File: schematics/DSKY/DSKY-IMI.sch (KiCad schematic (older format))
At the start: 3 parts, among them J103 Conn_02x08, J104 Conn_02x10, U201 74LS32

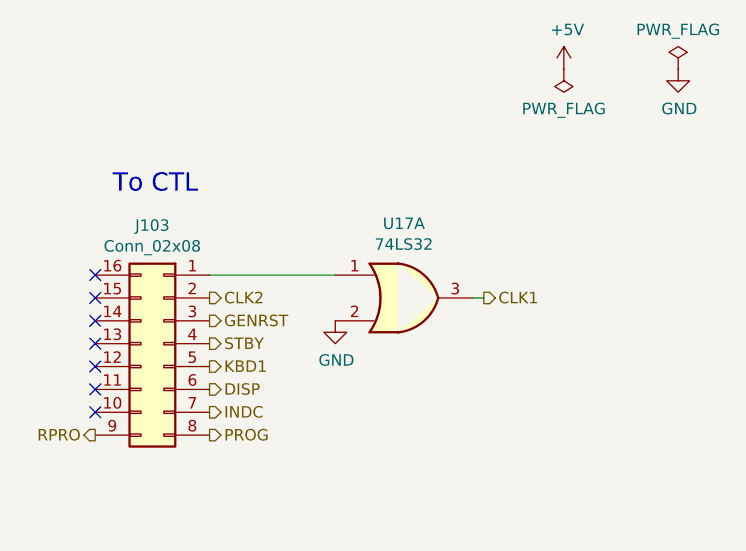
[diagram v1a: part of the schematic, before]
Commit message: Minor tweaks to the display decoding logic.
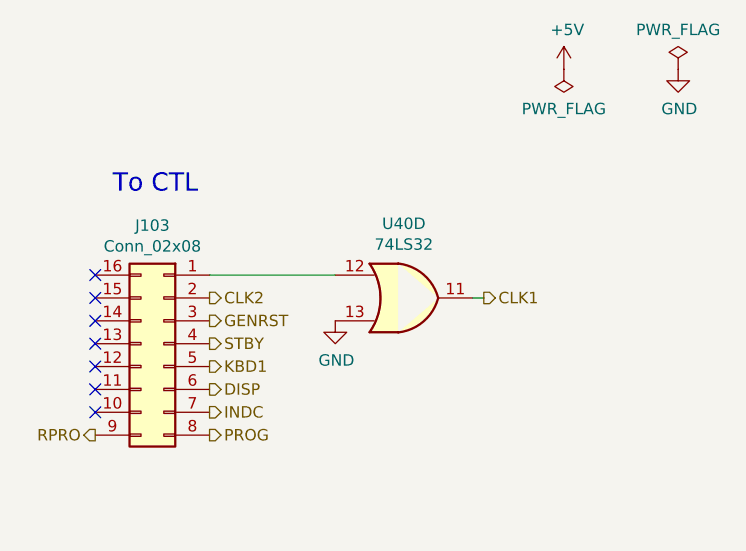
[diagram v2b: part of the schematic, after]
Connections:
- net CLK1: now also U201.11; no longer U201.3
- net GND: now also U201.13; no longer U201.2
- net at J103.1 (Pin_1): now also U201.12; no longer U201.1
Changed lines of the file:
@@
 $Comp
 L 74xx:74LS32 U201
-U 1 1 5F6065A8
+U 4 1 5F6065A8
 P 8400 2000
 AR Path="/5F5E4E3B/5F5F82D4/5F6065A8" Ref="U201"  Part="1"
-AR Path="/60F989FD/5F6065A8" Ref="U17"  Part="1"
-F 0 "U17" H 8400 2325 50  0000 C CNN
+AR Path="/60F989FD/5F6065A8" Ref="U40"  Part="4"
+F 0 "U40" H 8400 2325 50  0000 C CNN
 F 1 "74LS32" H 8400 2234 50  0000 C CNN
 F 2 "" H 8400 2000 50  0001 C CNN
 F 3 "http://www.ti.com/lit/gpn/sn74LS32" H 8400 2000 50  0001 C CNN
-	1    8400 2000
+	4    8400 2000
 	1    0    0    -1
 $EndComp

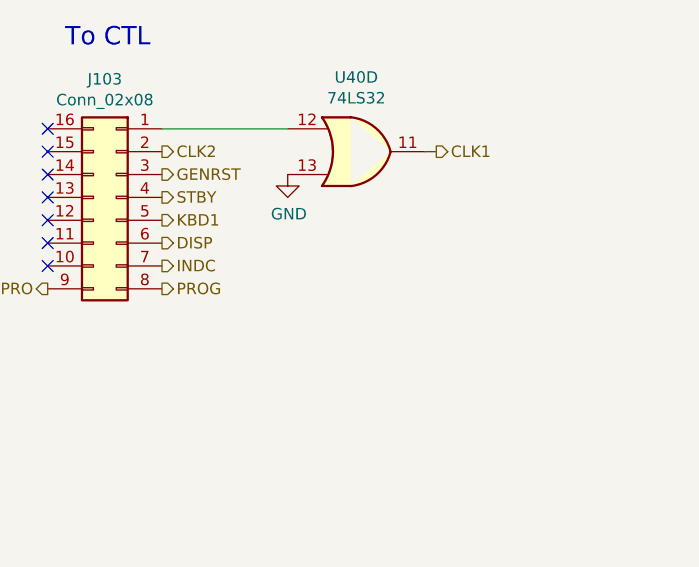
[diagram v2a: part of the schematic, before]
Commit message: Simplified reset lines.
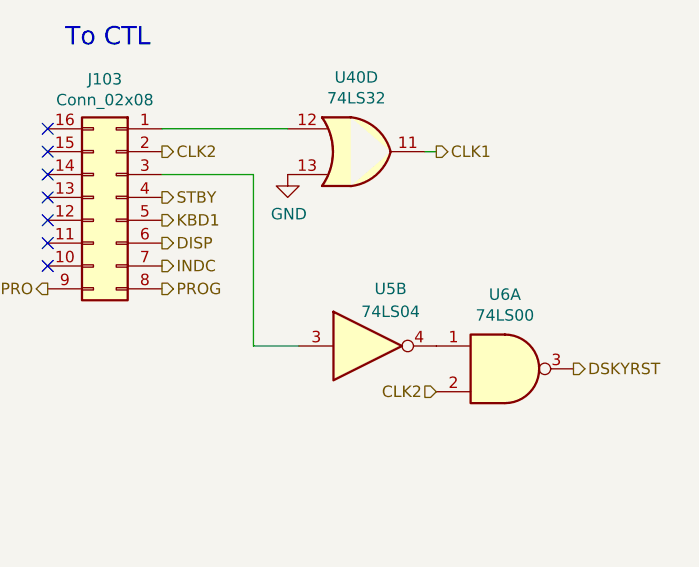
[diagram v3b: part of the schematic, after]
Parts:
- added U5: 74LS04, symbol 74xx:74LS04
- added U6: 74LS00, symbol 74xx:74LS00
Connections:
- net CLK2: now also U6.2
- net GENRST: no longer names the net of J103.3 (Pin_3)
- net GENRST: now also U5.3
- new net: U5.4, U6.1
- new net DSKYRST: U6.3
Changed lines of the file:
@@
 Text HLabel 8750 2000 2    50   Output ~ 0
 CLK1
-Text HLabel 7550 2100 2    50   Output ~ 0
-GENRST
 Wire Wire Line
 	4200 1750 3950 1750
@@
 Text HLabel 7050 2600 0    50   Output ~ 0
 RPRO
+Text HLabel 9350 2950 2    50   Output ~ 0
+DSKYRST
+Text HLabel 8750 3050 0    50   Input ~ 0
+CLK2
+$Comp
+L 74xx:74LS00 U?
+U 1 1 6395652F
+P 9050 2950
+AR Path="/5F5E4E3B/5F5F8347/6395652F" Ref="U?"  Part="1"
+AR Path="/60F98A72/6395652F" Ref="U?"  Part="1"
+AR Path="/66BEE9C8/6395652F" Ref="U?"  Part="1"
+AR Path="/60F98A72/66CE2F9E/6395652F" Ref="U?"  Part="1"
+AR Path="/60F989FD/6395652F" Ref="U6"  Part="1"
+F 0 "U6" H 9050 3275 50  0000 C CNN
+F 1 "74LS00" H 9050 3184 50  0000 C CNN
+F 2 "" H 9050 2950 50  0001 C CNN
+F 3 "http://www.ti.com/lit/gpn/sn74ls00" H 9050 2950 50  0001 C CNN
+	1    9050 2950
+	1    0    0    -1
+$EndComp
+$Comp
+L 74xx:74LS04 U?
+U 2 1 63956535
+P 8450 2850
+AR Path="/5F5E4E3B/5F5F8347/63956535" Ref="U?"  Part="6"
+AR Path="/60F98A72/63956535" Ref="U?"  Part="2"
+AR Path="/66BEE9C8/63956535" Ref="U?"  Part="6"
+AR Path="/60F98A72/66CE2F9E/63956535" Ref="U?"  Part="6"
+AR Path="/60F989FD/63956535" Ref="U5"  Part="2"
+F 0 "U5" H 8550 3100 50  0000 C CNN
+F 1 "74LS04" H 8550 3000 50  0000 C CNN
+F 2 "" H 8450 2850 50  0001 C CNN
+F 3 "http://www.ti.com/lit/gpn/sn74LS04" H 8450 2850 50  0001 C CNN
+	2    8450 2850
+	1    0    0    -1
+$EndComp
+Wire Wire Line
+	7550 2100 7950 2100
+Wire Wire Line
+	7950 2100 7950 2850
+Wire Wire Line
+	7950 2850 8150 2850
 Wire Bus Line
 	5100 2250 5100 2800

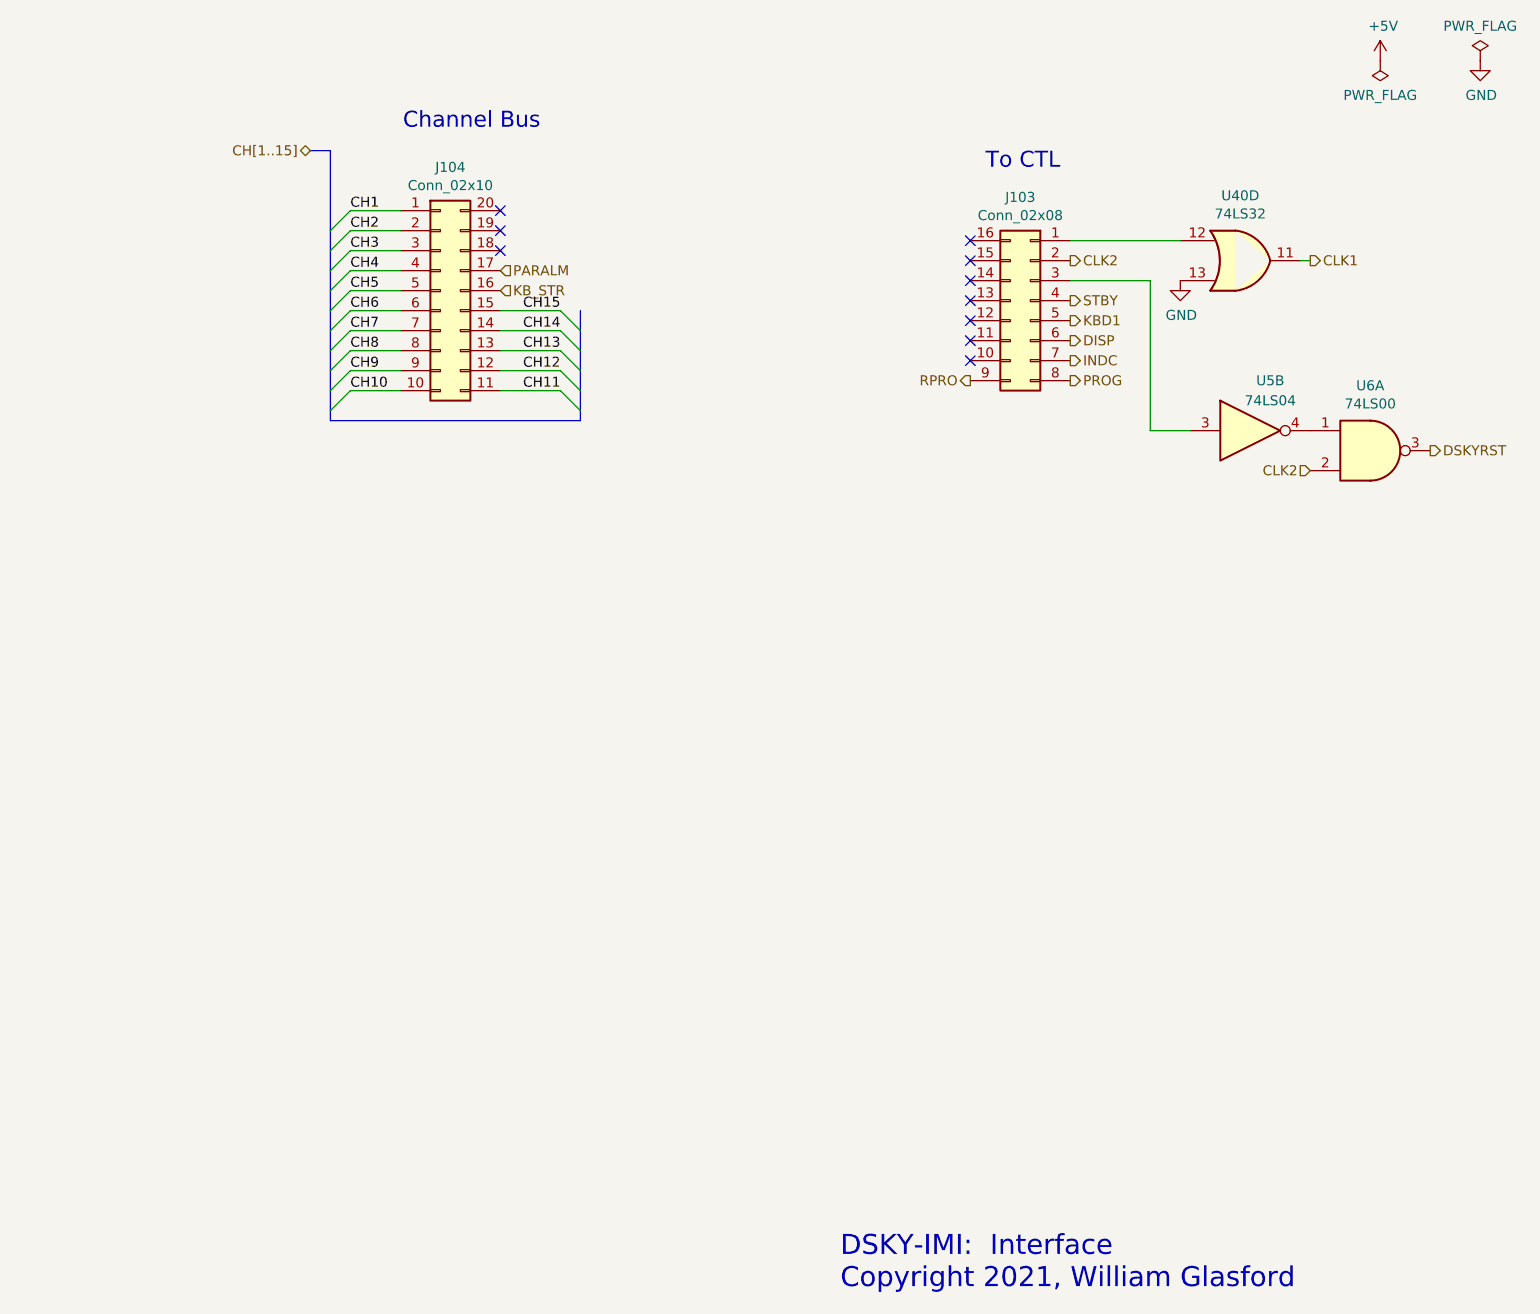
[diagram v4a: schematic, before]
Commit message: Overhauled the handling of the sign characters.
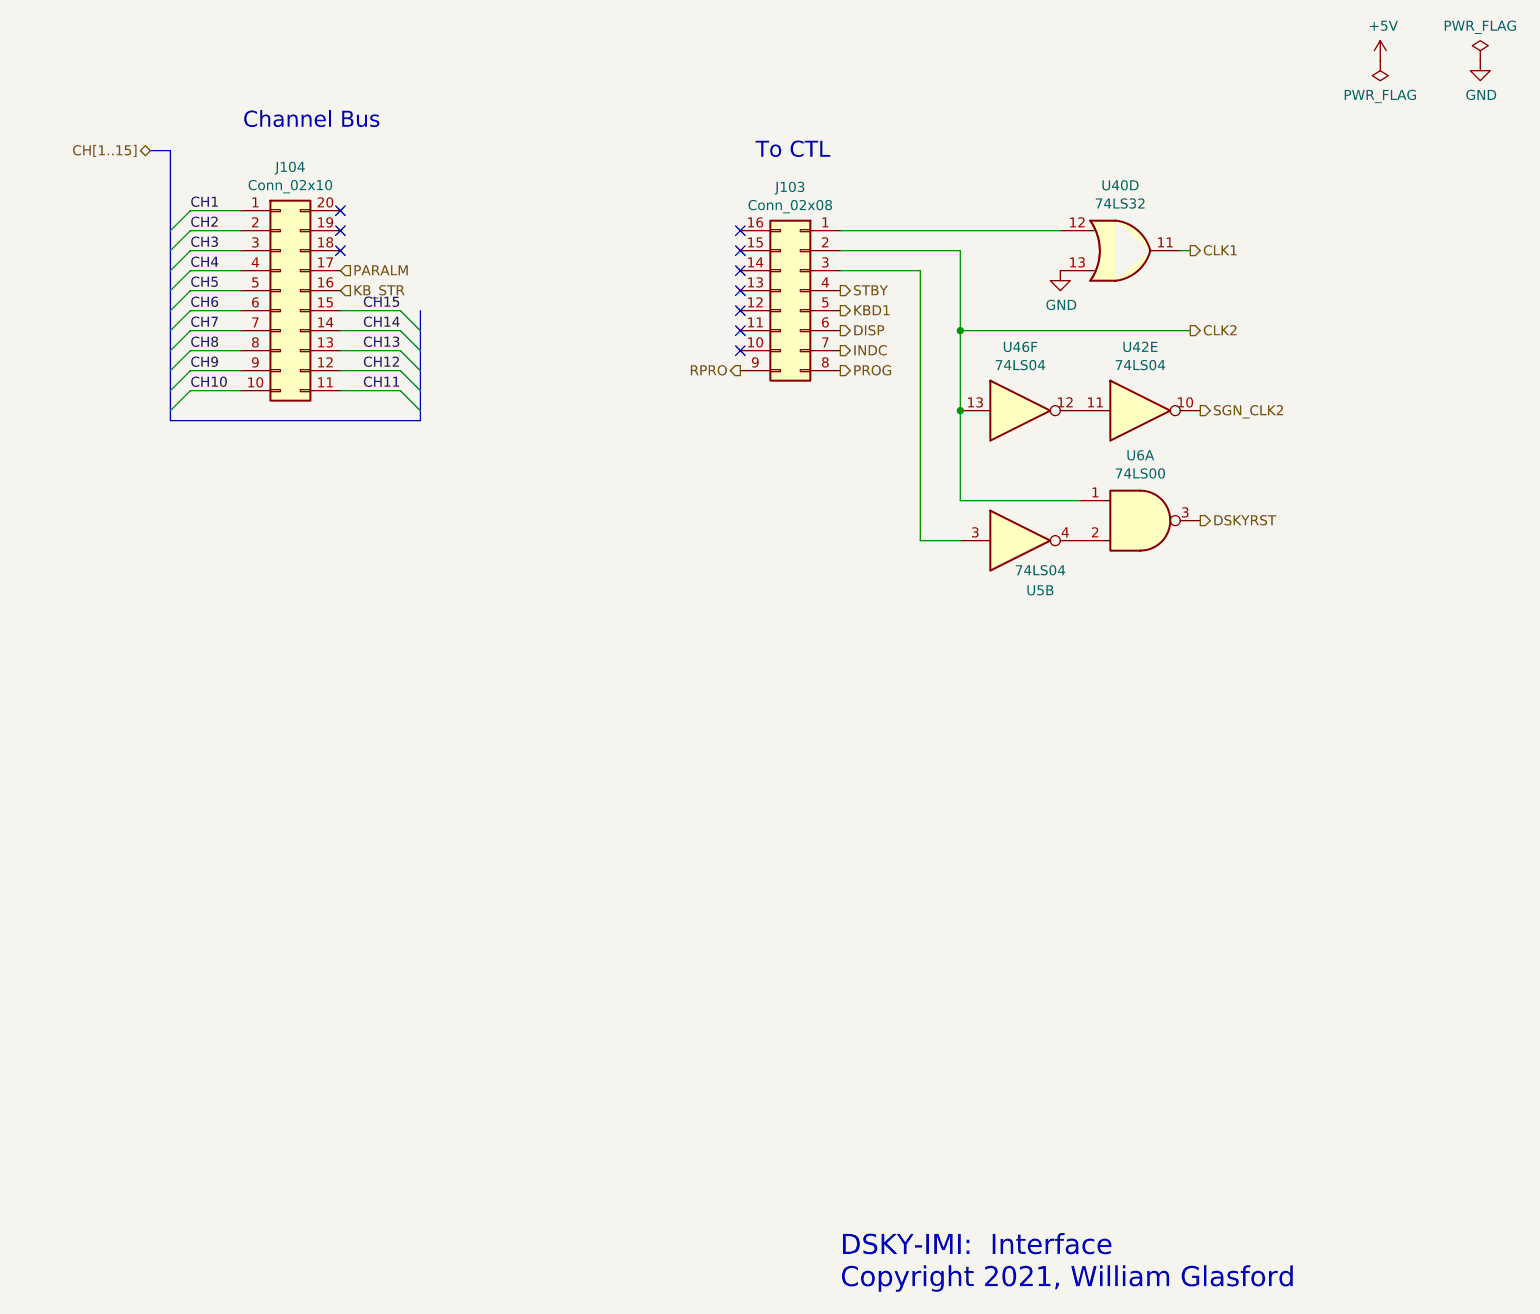
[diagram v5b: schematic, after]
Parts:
- added U42, U46: 74LS04, symbol 74xx:74LS04
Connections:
- net CLK2: now also U6.1, U46.13; no longer U6.2
- net at U5.4: now also U6.2; no longer U6.1
- new net: U42.11, U46.12
- new net SGN_CLK2: U42.10
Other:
- moved on the sheet: J103, J104, U40D, U5B, U6A

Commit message: Final tweaks, the DSKY is now complete!
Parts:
- removed U201: 74LS32, symbol 74xx:74LS32
- added U19: 74LS04, symbol 74xx:74LS04
- added unit 3 of U46
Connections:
- net CLK1: now also J103.1 (Pin_1)
- net KBD1: now also U46.6; no longer J103.5 (Pin_5)
- net STBY: now also U19.6; no longer J103.4 (Pin_4)
- net CLK3: now reaches J103.10 (Pin_10)
- new net: J103.4 (Pin_4), U19.5
- new net: J103.5 (Pin_5), U46.5
- no-connect marks 10 -> 9
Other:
- note added: "Note: PROG, RPRO & PARALM are Active High,\nthe rest are Active Low with the clock signals\nand KB_STR being pulses."
- moved on the sheet: U42E, U46F, U5B, U6A
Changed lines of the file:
@@
 Comment4 ""
 $EndDescr
-$Comp
-L power:GND #PWR0102
-U 1 1 5F61EFB4
-P 7500 2050
-AR Path="/5F5E4E3B/5F5F82D4/5F61EFB4" Ref="#PWR0102"  Part="1"
-AR Path="/60F989FD/5F61EFB4" Ref="#PWR0102"  Part="1"
-F 0 "#PWR0102" H 7500 1800 50  0001 C CNN
-F 1 "GND" H 7505 1877 50  0000 C CNN
-F 2 "" H 7500 2050 50  0001 C CNN
-F 3 "" H 7500 2050 50  0001 C CNN
-	1    7500 2050
-	1    0    0    -1
-$EndComp
-Wire Wire Line
-	8150 1950 8100 1950
-Text HLabel 8150 2350 2    50   Output ~ 0
+Text HLabel 7600 1950 2    50   Output ~ 0
 CLK2
-Text HLabel 8150 1950 2    50   Output ~ 0
+Text HLabel 6400 1850 2    50   Output ~ 0
 CLK1
 Wire Wire Line
@@
 Wire Wire Line
 	3900 2250 4200 2250
-Text HLabel 6400 2150 2    50   Output ~ 0
+Text HLabel 7700 3750 2    50   Output ~ 0
 STBY
 Text HLabel 3900 2150 2    50   Input ~ 0
@@
 Text Notes 6350 1500 2    80   ~ 0
 To CTL
-Text HLabel 6400 2250 2    50   Output ~ 0
+Text HLabel 7700 4400 2    50   Output ~ 0
 KBD1
 Text HLabel 6400 2350 2    50   Output ~ 0
@@
 INDC
 NoConn ~ 5900 2350
-NoConn ~ 5900 2450
-Wire Wire Line
-	6400 1850 7500 1850
 Wire Bus Line
 	4300 2800 3050 2800
-$Comp
-L 74xx:74LS32 U201
-U 4 1 5F6065A8
-P 7800 1950
-AR Path="/5F5E4E3B/5F5F82D4/5F6065A8" Ref="U201"  Part="1"
-AR Path="/60F989FD/5F6065A8" Ref="U40"  Part="4"
-F 0 "U40" H 7800 2275 50  0000 C CNN
-F 1 "74LS32" H 7800 2184 50  0000 C CNN
-F 2 "" H 7800 1950 50  0001 C CNN
-F 3 "http://www.ti.com/lit/gpn/sn74LS32" H 7800 1950 50  0001 C CNN
-	4    7800 1950
-	1    0    0    -1
-$EndComp
 Text Notes 6400 7150 0    100  ~ 0
 DSKY-IMI:  Interface\nCopyright 2021, William Glasford
@@
 Text HLabel 5900 2550 0    50   Output ~ 0
 RPRO
-Text HLabel 8200 3300 2    50   Output ~ 0
+Text HLabel 8650 3050 2    50   Output ~ 0
 DSKYRST
 $Comp
 L 74xx:74LS00 U?
 U 1 1 6395652F
-P 7900 3300
+P 8350 3050
 AR Path="/5F5E4E3B/5F5F8347/6395652F" Ref="U?"  Part="1"
 AR Path="/60F98A72/6395652F" Ref="U?"  Part="1"
@@
 AR Path="/60F98A72/66CE2F9E/6395652F" Ref="U?"  Part="1"
 AR Path="/60F989FD/6395652F" Ref="U6"  Part="1"
-F 0 "U6" H 7900 3625 50  0000 C CNN
-F 1 "74LS00" H 7900 3534 50  0000 C CNN
-F 2 "" H 7900 3300 50  0001 C CNN
-F 3 "http://www.ti.com/lit/gpn/sn74ls00" H 7900 3300 50  0001 C CNN
-	1    7900 3300
+F 0 "U6" H 8350 3375 50  0000 C CNN
+F 1 "74LS00" H 8350 3284 50  0000 C CNN
+F 2 "" H 8350 3050 50  0001 C CNN
+F 3 "http://www.ti.com/lit/gpn/sn74ls00" H 8350 3050 50  0001 C CNN
+	1    8350 3050
 	1    0    0    -1
 $EndComp
@@
 L 74xx:74LS04 U?
 U 2 1 63956535
-P 7300 3400
+P 7750 3150
 AR Path="/5F5E4E3B/5F5F8347/63956535" Ref="U?"  Part="6"
 AR Path="/60F98A72/63956535" Ref="U?"  Part="2"
@@
 AR Path="/60F98A72/66CE2F9E/63956535" Ref="U?"  Part="6"
 AR Path="/60F989FD/63956535" Ref="U5"  Part="2"
-F 0 "U5" H 7400 3150 50  0000 C CNN
-F 1 "74LS04" H 7400 3250 50  0000 C CNN
-F 2 "" H 7300 3400 50  0001 C CNN
-F 3 "http://www.ti.com/lit/gpn/sn74LS04" H 7300 3400 50  0001 C CNN
-	2    7300 3400
-	1    0    0    -1
-$EndComp
-Wire Wire Line
-	6400 2050 6800 2050
-Wire Wire Line
-	6800 2050 6800 3400
-Wire Wire Line
-	6800 3400 7000 3400
+F 0 "U5" H 7850 2900 50  0000 C CNN
+F 1 "74LS04" H 7850 3000 50  0000 C CNN
+F 2 "" H 7750 3150 50  0001 C CNN
+F 3 "http://www.ti.com/lit/gpn/sn74LS04" H 7750 3150 50  0001 C CNN
+	2    7750 3150
+	1    0    0    -1
+$EndComp
+Wire Wire Line
+	6400 2050 7250 2050
+Wire Wire Line
+	7250 2050 7250 3150
+Wire Wire Line
+	7250 3150 7450 3150
 $Comp
 L 74xx:74LS04 U42
 U 5 1 6247150B
-P 7900 2750
-F 0 "U42" H 7900 3067 50  0000 C CNN
-F 1 "74LS04" H 7900 2976 50  0000 C CNN
-F 2 "" H 7900 2750 50  0001 C CNN
-F 3 "http://www.ti.com/lit/gpn/sn74LS04" H 7900 2750 50  0001 C CNN
-	5    7900 2750
+P 8350 2500
+F 0 "U42" H 8350 2817 50  0000 C CNN
+F 1 "74LS04" H 8350 2726 50  0000 C CNN
+F 2 "" H 8350 2500 50  0001 C CNN
+F 3 "http://www.ti.com/lit/gpn/sn74LS04" H 8350 2500 50  0001 C CNN
+	5    8350 2500
 	1    0    0    -1
 $EndComp
@@
 L 74xx:74LS04 U46
 U 6 1 62471E0E
-P 7300 2750
-F 0 "U46" H 7300 3067 50  0000 C CNN
-F 1 "74LS04" H 7300 2976 50  0000 C CNN
-F 2 "" H 7300 2750 50  0001 C CNN
-F 3 "http://www.ti.com/lit/gpn/sn74LS04" H 7300 2750 50  0001 C CNN
-	6    7300 2750
-	1    0    0    -1
-$EndComp
-Wire Wire Line
-	6400 1950 7000 1950
-Wire Wire Line
-	7000 1950 7000 2350
-Wire Wire Line
-	8150 2350 7000 2350
-Connection ~ 7000 2350
-Wire Wire Line
-	7000 2350 7000 2750
-Wire Wire Line
-	7000 2750 7000 3200
-Wire Wire Line
-	7000 3200 7600 3200
-Connection ~ 7000 2750
-Text HLabel 8200 2750 2    50   Output ~ 0
+P 7750 2500
+F 0 "U46" H 7750 2817 50  0000 C CNN
+F 1 "74LS04" H 7750 2726 50  0000 C CNN
+F 2 "" H 7750 2500 50  0001 C CNN
+F 3 "http://www.ti.com/lit/gpn/sn74LS04" H 7750 2500 50  0001 C CNN
+	6    7750 2500
+	1    0    0    -1
+$EndComp
+Wire Wire Line
+	6400 1950 7450 1950
+Wire Wire Line
+	7600 1950 7450 1950
+Wire Wire Line
+	7450 2950 8050 2950
+Text HLabel 8650 2500 2    50   Output ~ 0
 SGN_CLK2
+Wire Wire Line
+	7450 1950 7450 2500
+Connection ~ 7450 1950
+Connection ~ 7450 2500
+Wire Wire Line
+	7450 2500 7450 2950
+Text Notes 3350 3700 0    70   ~ 0
+Note: PROG, RPRO & PARALM are Active High,\nthe rest are Active Low with the clock signals\nand KB_STR being pulses.
+$Comp
+L 74xx:74LS04 U19
+U 3 1 61EE72FE
+P 7400 3750
+F 0 "U19" H 7400 4067 50  0000 C CNN
+F 1 "74LS04" H 7400 3976 50  0000 C CNN
+F 2 "" H 7400 3750 50  0001 C CNN
+F 3 "http://www.ti.com/lit/gpn/sn74LS04" H 7400 3750 50  0001 C CNN
+	3    7400 3750
+	1    0    0    -1
+$EndComp
+Wire Wire Line
+	6400 2150 7100 2150
+Wire Wire Line
+	7100 2150 7100 3750
+$Comp
+L 74xx:74LS04 U46
+U 3 1 61F122AA
+P 7400 4400
+F 0 "U46" H 7400 4717 50  0000 C CNN
+F 1 "74LS04" H 7400 4626 50  0000 C CNN
+F 2 "" H 7400 4400 50  0001 C CNN
+F 3 "http://www.ti.com/lit/gpn/sn74LS04" H 7400 4400 50  0001 C CNN
+	3    7400 4400
+	1    0    0    -1
+$EndComp
+Wire Wire Line
+	6400 2250 6950 2250
+Wire Wire Line
+	6950 2250 6950 4400
+Wire Wire Line
+	6950 4400 7100 4400
 Wire Bus Line
 	4300 2250 4300 2800
 Wire Bus Line
 	3050 1450 3050 2800
+Text HLabel 5900 2450 0    50   Output ~ 0
+CLK3
 $EndSCHEMATC
